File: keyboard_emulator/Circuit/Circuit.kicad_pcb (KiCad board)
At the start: 2 copper layers, 1 part, among them U1 Sparkfun_Pro_Micro

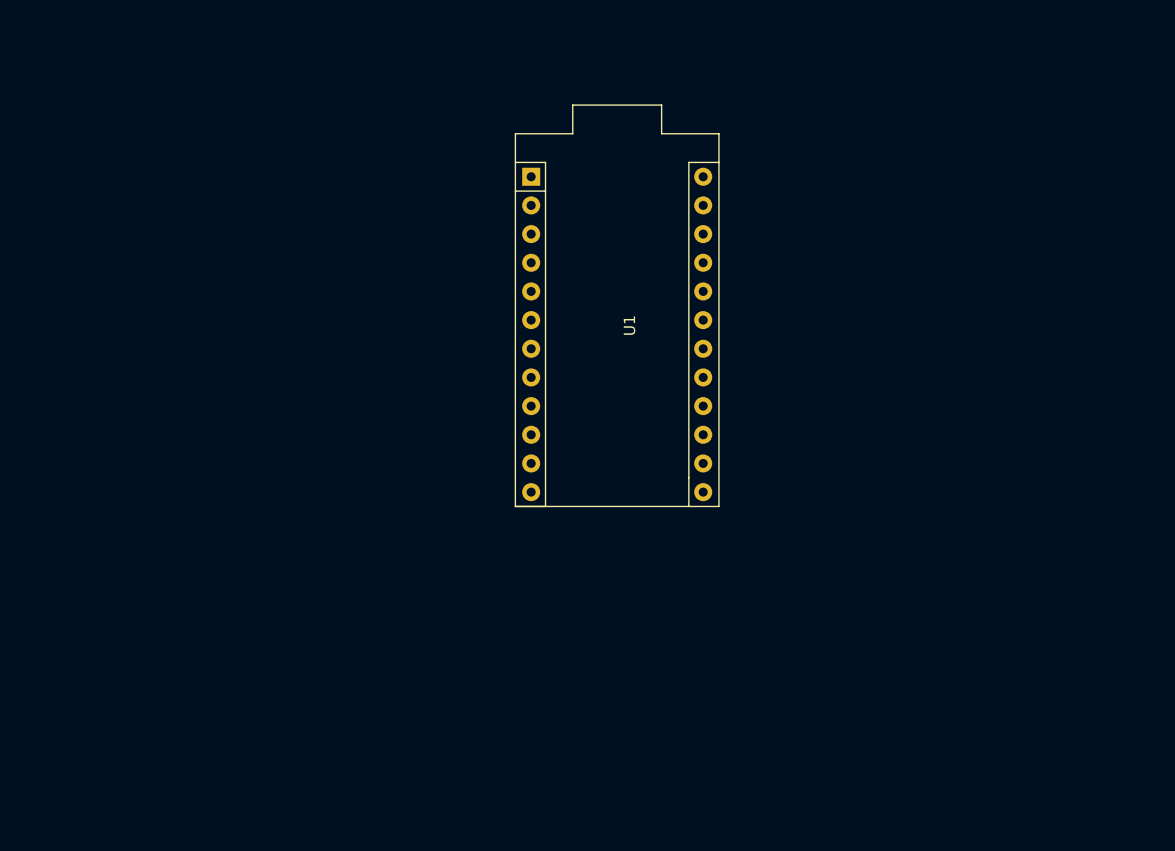
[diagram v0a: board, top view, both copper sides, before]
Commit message: finished keyboard emulator circuit and some BOMs
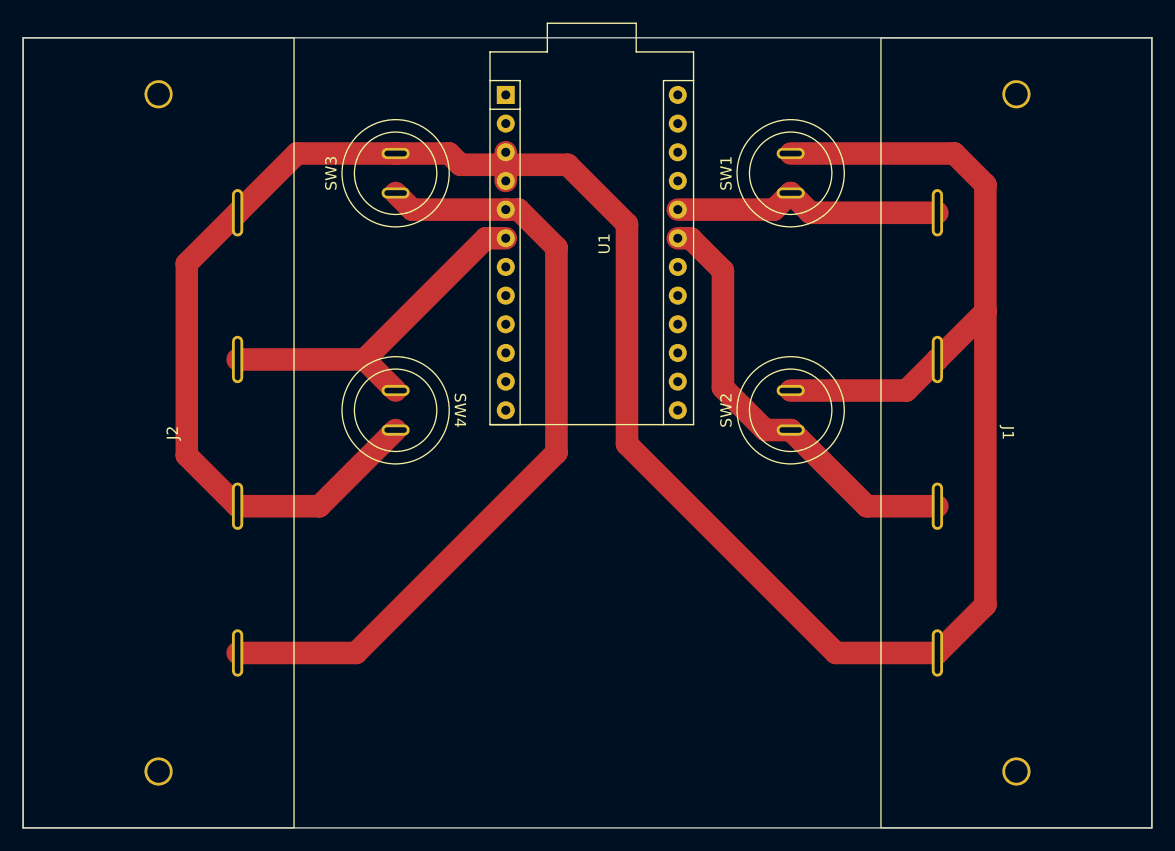
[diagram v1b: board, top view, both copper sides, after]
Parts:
- added J1: Screw_Terminal_01x04, speaker_terminal_spring:speaker_terminal_spring_4, F.Cu at (190.0, 102.0)
- added J2: Screw_Terminal_01x04, speaker_terminal_spring:speaker_terminal_spring_4, F.Cu at (114.0, 102.0)
- added SW1: SW_Push, push_button_big_oval:push_button_oval, F.Cu at (170.0, 79.0)
- added SW2: SW_Push, push_button_big_oval:push_button_oval, F.Cu at (170.0, 100.0)
- added SW3: SW_Push, push_button_big_oval:push_button_oval, F.Cu at (135.0, 79.0)
- added SW4: SW_Push, push_button_big_oval:push_button_oval, F.Cu at (135.0, 100.0)
- moved U1 7.59 mm to (160.0, 100.0)
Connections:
- U1 pad 19: unconnected-(U1-D20/A2-Pad19) -> Button4
- U1 pad 20: unconnected-(U1-D21/A3-Pad20) -> Button3
- U1 pad 3: unconnected-(U1-GND-Pad3) -> GND
- U1 pad 4: unconnected-(U1-GND-Pad4) -> GND
- U1 pad 5: unconnected-(U1-D2-Pad5) -> Button1
- U1 pad 6: unconnected-(U1-~D3-Pad6) -> Button2
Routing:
- net GND: track 0.00 -> 225.1 mm
- net Button1: track 0.00 -> 70.0 mm
- net Button4: track 0.00 -> 38.9 mm
- net Button2: track 0.00 -> 32.1 mm
- net Button3: track 0.00 -> 24.3 mm
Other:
- board outline added: 100 x 70 mm
